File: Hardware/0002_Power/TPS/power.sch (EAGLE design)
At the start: 16 parts

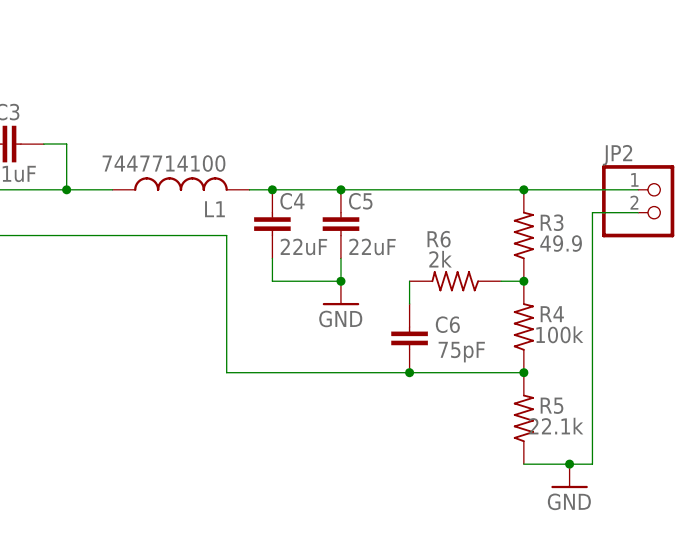
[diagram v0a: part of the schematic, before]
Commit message: RF power updated schematic & board (in progress)
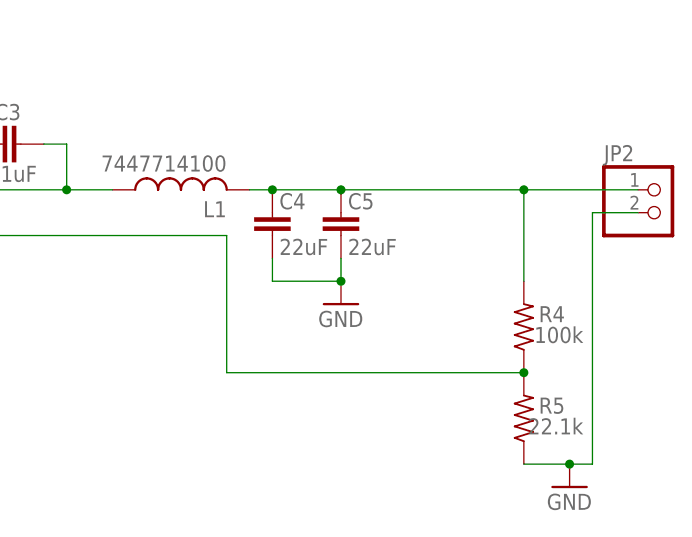
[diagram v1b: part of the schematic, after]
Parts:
- removed C6: 75pF, rcl:C-EUC2012
- removed R3: 49.9, rcl:R-US_R0805
- removed R6: 2k, rcl:R-US_R0805
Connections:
- removed net N$5: R3.1, R4.2, R6.1
- removed net N$7: C6.1, R6.2
- net N$4: now also R4.2; no longer R3.2
- net N$8: no longer C6.2
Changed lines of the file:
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@@
 <part name="C5" library="rcl" library_urn="urn:adsk.eagle:library:334" deviceset="C-EU" device="C2012" package3d_urn="urn:adsk.eagle:package:23625/2" value="22uF"/>
 <part name="GND6" library="supply1" library_urn="urn:adsk.eagle:library:371" deviceset="GND" device=""/>
-<part name="R3" library="rcl" library_urn="urn:adsk.eagle:library:334" deviceset="R-US_" device="R0805" package3d_urn="urn:adsk.eagle:package:23553/2" value="49.9"/>
 <part name="R4" library="rcl" library_urn="urn:adsk.eagle:library:334" deviceset="R-US_" device="R0805" package3d_urn="urn:adsk.eagle:package:23553/2" value="100k"/>
 <part name="R5" library="rcl" library_urn="urn:adsk.eagle:library:334" deviceset="R-US_" device="R0805" package3d_urn="urn:adsk.eagle:package:23553/2" value="22.1k"/>
-<part name="R6" library="rcl" library_urn="urn:adsk.eagle:library:334" deviceset="R-US_" device="R0805" package3d_urn="urn:adsk.eagle:package:23553/2" value="2k"/>
-<part name="C6" library="rcl" library_urn="urn:adsk.eagle:library:334" deviceset="C-EU" device="C2012" package3d_urn="urn:adsk.eagle:package:23625/2" value="75pF"/>
 <part name="GND2" library="supply1" library_urn="urn:adsk.eagle:library:371" deviceset="GND" device=""/>
 </parts>
@@
 <attribute name="VALUE" x="91.44" y="48.26" size="1.778" layer="96"/>
 </instance>
-<instance part="R3" gate="G$1" x="114.3" y="58.42" smashed="yes" rot="R90">
-<attribute name="NAME" x="118.872" y="60.7314" size="1.778" layer="95" rot="R180"/>
-<attribute name="VALUE" x="120.904" y="58.42" size="1.778" layer="96" rot="R180"/>
-</instance>
 <instance part="R4" gate="G$1" x="114.3" y="48.26" smashed="yes" rot="R90">
 <attribute name="NAME" x="118.872" y="50.5714" size="1.778" layer="95" rot="R180"/>
@@
 <attribute name="NAME" x="118.872" y="40.4114" size="1.778" layer="95" rot="R180"/>
 <attribute name="VALUE" x="120.904" y="38.1" size="1.778" layer="96" rot="R180"/>
-</instance>
-<instance part="R6" gate="G$1" x="106.68" y="53.34" smashed="yes" rot="R180">
-<attribute name="NAME" x="103.378" y="57.1246" size="1.778" layer="95"/>
-<attribute name="VALUE" x="103.632" y="54.864" size="1.778" layer="96"/>
-</instance>
-<instance part="C6" gate="G$1" x="101.6" y="48.26" smashed="yes">
-<attribute name="NAME" x="104.394" y="47.625" size="1.778" layer="95"/>
-<attribute name="VALUE" x="104.648" y="44.831" size="1.778" layer="96"/>
 </instance>
 <instance part="GND2" gate="1" x="119.38" y="30.48" smashed="yes">
@@
 <wire x1="93.98" y1="63.5" x2="114.3" y2="63.5" width="0.1524" layer="91"/>
 <junction x="93.98" y="63.5"/>
-<pinref part="R3" gate="G$1" pin="2"/>
+<pinref part="R4" gate="G$1" pin="2"/>
 <wire x1="114.3" y1="63.5" x2="127" y2="63.5" width="0.1524" layer="91"/>
+<wire x1="114.3" y1="63.5" x2="114.3" y2="53.34" width="0.1524" layer="91"/>
 <junction x="114.3" y="63.5"/>
-</segment>
-</net>
-<net name="N$5" class="0">
-<segment>
-<pinref part="R3" gate="G$1" pin="1"/>
-<pinref part="R4" gate="G$1" pin="2"/>
-<pinref part="R6" gate="G$1" pin="1"/>
-<wire x1="111.76" y1="53.34" x2="114.3" y2="53.34" width="0.1524" layer="91"/>
-<junction x="114.3" y="53.34"/>
-</segment>
-</net>
-<net name="N$7" class="0">
-<segment>
-<pinref part="R6" gate="G$1" pin="2"/>
-<pinref part="C6" gate="G$1" pin="1"/>
-<wire x1="101.6" y1="53.34" x2="101.6" y2="50.8" width="0.1524" layer="91"/>
 </segment>
 </net>
@@
 <pinref part="R5" gate="G$1" pin="2"/>
 <junction x="114.3" y="43.18"/>
-<wire x1="114.3" y1="43.18" x2="101.6" y2="43.18" width="0.1524" layer="91"/>
-<pinref part="C6" gate="G$1" pin="2"/>
 <pinref part="U$2" gate="G$1" pin="FB"/>
 <wire x1="53.34" y1="58.42" x2="81.28" y2="58.42" width="0.1524" layer="91"/>
 <wire x1="81.28" y1="58.42" x2="81.28" y2="43.18" width="0.1524" layer="91"/>
-<wire x1="81.28" y1="43.18" x2="101.6" y2="43.18" width="0.1524" layer="91"/>
-<junction x="101.6" y="43.18"/>
-</segment>
-</net>
+<wire x1="81.28" y1="43.18" x2="114.3" y2="43.18" width="0.1524" layer="91"/>
+</segment>
+</net>
